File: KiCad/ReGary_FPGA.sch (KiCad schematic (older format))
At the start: 28 parts, among them U1 GW1N-UV1P5LQ100, U2 LM1117-3.3, U3 TPS73643DBV

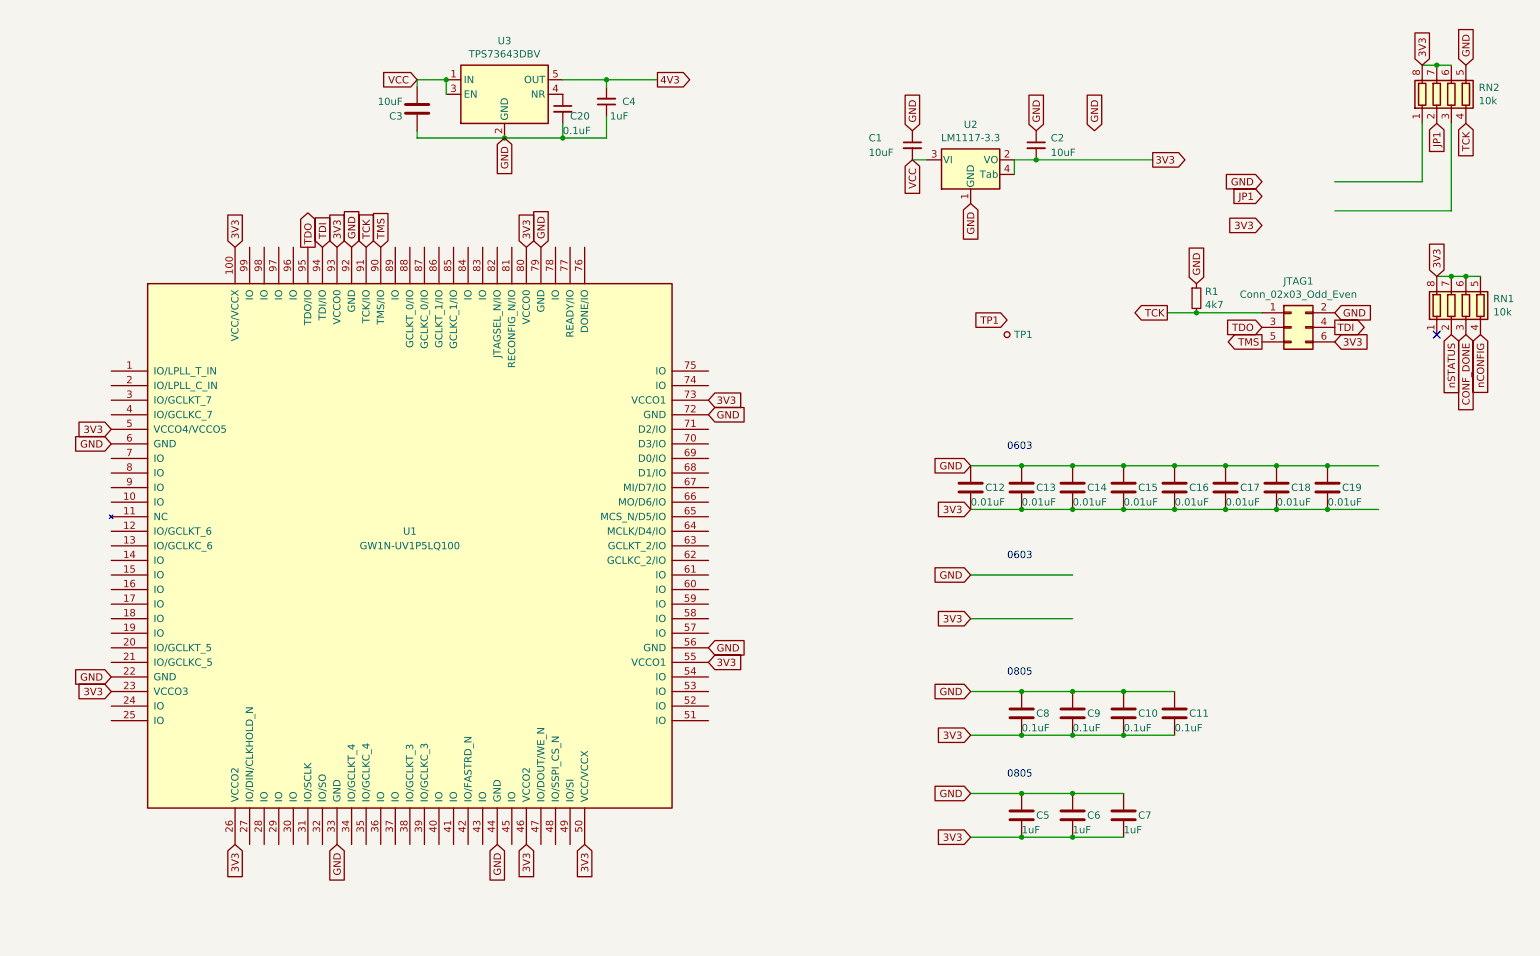
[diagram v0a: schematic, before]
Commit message: Add JP header for JTAGSEL_N, fixed JTAG as dual-purpose pins
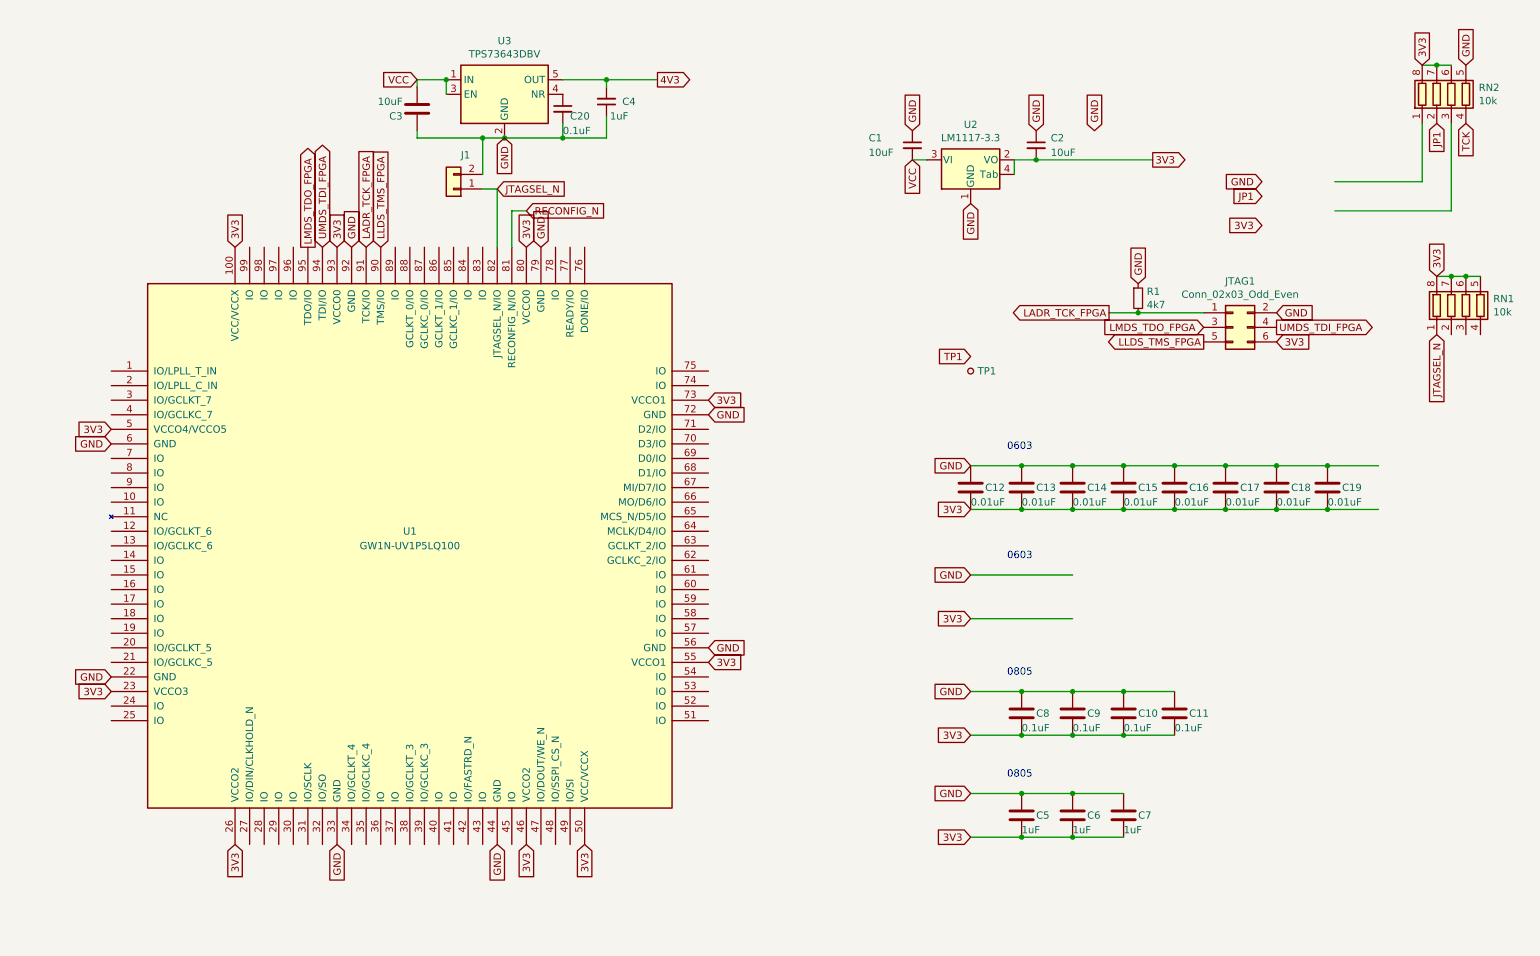
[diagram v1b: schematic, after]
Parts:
- added J1: Conn_01x02, Connector_PinHeader_2.00mm:PinHeader_1x02_P2.00mm_Vertical, symbol Connector_Generic:Conn_01x02
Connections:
- net labels added: JTAGSEL_N, LADR_TCK_FPGA, LLDS_TMS_FPGA, LMDS_TDO_FPGA, RECONFIG_N, UMDS_TDI_FPGA
- net labels removed: CONF_DONE, TDI, TDO, TMS, nCONFIG, nSTATUS
- wire segments 59 -> 65
- no-connect marks 1 -> 0
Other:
- moved on the sheet: JTAG1, R1, TP1
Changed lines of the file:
@@
 Text GLabel 9250 1950 0    50   Input ~ 0
 3V3
-Text GLabel 8800 2350 1    50   Input ~ 0
-GND
-Text GLabel 2800 2100 1    50   Input ~ 0
-TDI
-Text GLabel 3200 2100 1    50   Input ~ 0
-TMS
-Text GLabel 2700 2100 1    50   Output ~ 0
-TDO
+Text GLabel 8400 2350 1    50   Input ~ 0
+GND
 Text GLabel 10350 850  1    50   Input ~ 0
 3V3
@@
 	1    0    0    -1
 $EndComp
-Text GLabel 10650 2700 3    50   Input ~ 0
-CONF_DONE
-Text GLabel 10550 2700 3    50   Input ~ 0
-nSTATUS
-Text GLabel 10750 2700 3    50   Input ~ 0
-nCONFIG
 Text GLabel 10450 2300 1    50   Input ~ 0
 3V3
@@
 GND
 Text GLabel 10650 1250 3    50   Input ~ 0
-TCK
-Text GLabel 3100 2100 1    50   Input ~ 0
 TCK
 $Comp
@@
 	-1   0    0    1
 $EndComp
-Text GLabel 7500 2600 0    50   Input ~ 0
+Text GLabel 7250 2850 0    50   Input ~ 0
 TP1
 Wire Wire Line
@@
 L Connector:TestPoint_Small TP1
 U 1 1 655D4DC6
-P 7500 2700
-F 0 "TP1" H 7548 2700 50  0000 L CNN
-F 1 "TestPoint_Small" H 7548 2655 50  0001 L CNN
-F 2 "TestPoint:TestPoint_Pad_1.5x1.5mm" H 7700 2700 50  0001 C CNN
-F 3 "~" H 7700 2700 50  0001 C CNN
-	1    7500 2700
+P 7250 2950
+F 0 "TP1" H 7298 2950 50  0000 L CNN
+F 1 "TestPoint_Small" H 7298 2905 50  0001 L CNN
+F 2 "TestPoint:TestPoint_Pad_1.5x1.5mm" H 7450 2950 50  0001 C CNN
+F 3 "~" H 7450 2950 50  0001 C CNN
+	1    7250 2950
 	1    0    0    -1
 $EndComp
@@
 Wire Wire Line
 	10550 1250 10550 1850
-NoConn ~ 10450 2700
 $Comp
 L Device:C_Small C?
@@
 L Connector_Generic:Conn_02x03_Odd_Even JTAG1
 U 1 1 67CA7A4E
-P 9450 2650
-F 0 "JTAG1" H 9500 2967 50  0000 C CNN
-F 1 "Conn_02x03_Odd_Even" H 9500 2876 50  0000 C CNN
-F 2 "Connector_PinHeader_2.00mm:PinHeader_2x03_P2.00mm_Vertical_SMD" H 9450 2650 50  0001 C CNN
-F 3 "~" H 9450 2650 50  0001 C CNN
-	1    9450 2650
-	1    0    0    -1
-$EndComp
-Text GLabel 8600 2550 0    50   Output ~ 0
-TCK
-Text GLabel 9250 2650 0    50   Input ~ 0
-TDO
-Text GLabel 9250 2750 0    50   Output ~ 0
-TMS
-Text GLabel 9750 2550 2    50   Input ~ 0
-GND
-Text GLabel 9750 2650 2    50   Output ~ 0
-TDI
-Text GLabel 9750 2750 2    50   Input ~ 0
+P 9050 2650
+F 0 "JTAG1" H 9100 2967 50  0000 C CNN
+F 1 "Conn_02x03_Odd_Even" H 9100 2876 50  0000 C CNN
+F 2 "Connector_PinHeader_2.00mm:PinHeader_2x03_P2.00mm_Vertical_SMD" H 9050 2650 50  0001 C CNN
+F 3 "~" H 9050 2650 50  0001 C CNN
+	1    9050 2650
+	1    0    0    -1
+$EndComp
+Text GLabel 9350 2550 2    50   Input ~ 0
+GND
+Text GLabel 9350 2750 2    50   Input ~ 0
 3V3
 $Comp
@@
 	7700 1500 8500 1500
 Wire Wire Line
-	3450 1350 4050 1350
+	3450 1350 3900 1350
 Text GLabel 4050 1350 3    50   Input ~ 0
 GND
@@
 L Device:R_Small R1
 U 1 1 67F65041
-P 8800 2450
-F 0 "R1" H 8859 2496 50  0000 L CNN
-F 1 "4k7" H 8859 2405 50  0000 L CNN
-F 2 "Resistor_SMD:R_0603_1608Metric_Pad0.98x0.95mm_HandSolder" H 8800 2450 50  0001 C CNN
-F 3 "~" H 8800 2450 50  0001 C CNN
-	1    8800 2450
-	1    0    0    -1
-$EndComp
-Wire Wire Line
-	9250 2550 8800 2550
-Connection ~ 8800 2550
-Wire Wire Line
-	8800 2550 8600 2550
+P 8400 2450
+F 0 "R1" H 8459 2496 50  0000 L CNN
+F 1 "4k7" H 8459 2405 50  0000 L CNN
+F 2 "Resistor_SMD:R_0603_1608Metric_Pad0.98x0.95mm_HandSolder" H 8400 2450 50  0001 C CNN
+F 3 "~" H 8400 2450 50  0001 C CNN
+	1    8400 2450
+	1    0    0    -1
+$EndComp
+Wire Wire Line
+	8850 2550 8400 2550
+Connection ~ 8400 2550
+Wire Wire Line
+	8400 2550 8200 2550
 Wire Wire Line
 	8300 5150 8650 5150
@@
 	8300 5450 8650 5450
 Connection ~ 8300 5450
+Text GLabel 4000 1700 2    50   Input ~ 0
+JTAGSEL_N
+Text GLabel 10450 2700 3    50   Input ~ 0
+JTAGSEL_N
+$Comp
+L Connector_Generic:Conn_01x02 J1
+U 1 1 67FA6DF8
+P 3700 1700
+F 0 "J1" H 3618 1467 50  0000 C CNN
+F 1 "Conn_01x02" H 3618 1466 50  0001 C CNN
+F 2 "Connector_PinHeader_2.00mm:PinHeader_1x02_P2.00mm_Vertical" H 3700 1700 50  0001 C CNN
+F 3 "~" H 3700 1700 50  0001 C CNN
+	1    3700 1700
+	-1   0    0    1
+$EndComp
+Wire Wire Line
+	4100 2100 4100 1850
+Wire Wire Line
+	4100 1850 4200 1850
+Text GLabel 4200 1850 2    50   Input ~ 0
+RECONFIG_N
+Wire Wire Line
+	4000 2100 4000 1700
+Wire Wire Line
+	3900 1700 4000 1700
+Wire Wire Line
+	3900 1600 3900 1350
+Connection ~ 3900 1350
+Wire Wire Line
+	3900 1350 4050 1350
+Text GLabel 2800 2100 1    50   BiDi ~ 0
+UMDS_TDI_FPGA
+Text GLabel 9350 2650 2    50   Output ~ 0
+UMDS_TDI_FPGA
+Text GLabel 8850 2650 0    50   Input ~ 0
+LMDS_TDO_FPGA
+Text GLabel 2700 2100 1    50   Output ~ 0
+LMDS_TDO_FPGA
+Text GLabel 8200 2550 0    50   Output ~ 0
+LADR_TCK_FPGA
+Text GLabel 3100 2100 1    50   Input ~ 0
+LADR_TCK_FPGA
+Text GLabel 8850 2750 0    50   Output ~ 0
+LLDS_TMS_FPGA
+Text GLabel 3200 2100 1    50   Input ~ 0
+LLDS_TMS_FPGA
 $EndSCHEMATC

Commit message: More signal to pin assignments and routing
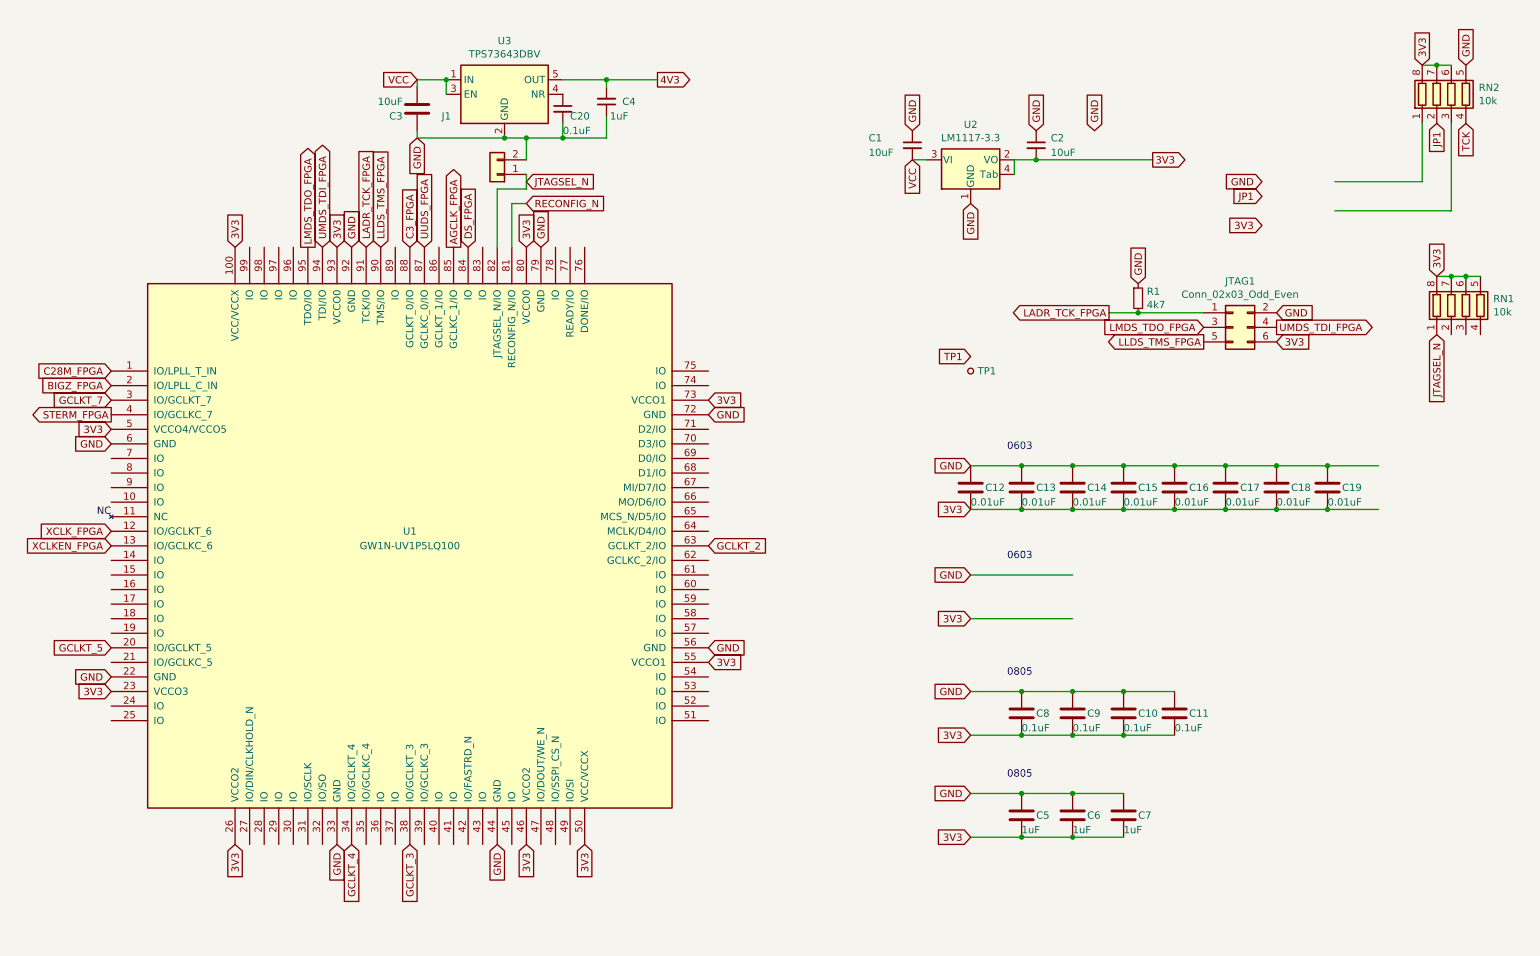
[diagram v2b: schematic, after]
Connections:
- net labels added: AGCLK_FPGA, BIGZ_FPGA, C28M_FPGA, C3_FPGA, DS_FPGA, GCLKT_2, GCLKT_3, GCLKT_4, GCLKT_5, GCLKT_7, NC, STERM_FPGA, UUDS_FPGA, XCLKEN_FPGA, XCLK_FPGA
- wire segments 65 -> 66
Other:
- moved on the sheet: J1
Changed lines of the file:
@@
 Wire Wire Line
 	7700 1500 8500 1500
-Wire Wire Line
-	3450 1350 3900 1350
-Text GLabel 4050 1350 3    50   Input ~ 0
+Text GLabel 3450 1350 3    50   Input ~ 0
 GND
 Text GLabel 5100 950  2    50   Output ~ 0
@@
 Wire Wire Line
 	3450 950  3450 1000
-Wire Wire Line
-	4050 1350 4450 1350
 Wire Wire Line
 	4750 1350 4750 1200
@@
 	8300 5450 8650 5450
 Connection ~ 8300 5450
-Text GLabel 4000 1700 2    50   Input ~ 0
+Text GLabel 4200 1650 2    50   Input ~ 0
 JTAGSEL_N
 Text GLabel 10450 2700 3    50   Input ~ 0
@@
 L Connector_Generic:Conn_01x02 J1
 U 1 1 67FA6DF8
-P 3700 1700
-F 0 "J1" H 3618 1467 50  0000 C CNN
-F 1 "Conn_01x02" H 3618 1466 50  0001 C CNN
-F 2 "Connector_PinHeader_2.00mm:PinHeader_1x02_P2.00mm_Vertical" H 3700 1700 50  0001 C CNN
-F 3 "~" H 3700 1700 50  0001 C CNN
-	1    3700 1700
+P 4000 1600
+F 0 "J1" H 4350 1200 50  0000 C CNN
+F 1 "Conn_01x02" H 3918 1366 50  0001 C CNN
+F 2 "Connector_PinHeader_2.00mm:PinHeader_1x02_P2.00mm_Vertical" H 4000 1600 50  0001 C CNN
+F 3 "~" H 4000 1600 50  0001 C CNN
+	1    4000 1600
 	-1   0    0    1
 $EndComp
-Wire Wire Line
-	4100 2100 4100 1850
-Wire Wire Line
-	4100 1850 4200 1850
-Text GLabel 4200 1850 2    50   Input ~ 0
+Text GLabel 4200 1800 2    50   Input ~ 0
 RECONFIG_N
-Wire Wire Line
-	4000 2100 4000 1700
-Wire Wire Line
-	3900 1700 4000 1700
-Wire Wire Line
-	3900 1600 3900 1350
-Connection ~ 3900 1350
-Wire Wire Line
-	3900 1350 4050 1350
 Text GLabel 2800 2100 1    50   BiDi ~ 0
 UMDS_TDI_FPGA
@@
 Text GLabel 3200 2100 1    50   Input ~ 0
 LLDS_TMS_FPGA
+Text GLabel 1350 4050 0    50   Input ~ 0
+XCLK_FPGA
+Text GLabel 3400 2100 1    50   Input ~ 0
+C3_FPGA
+Wire Wire Line
+	4200 1800 4100 1800
+Wire Wire Line
+	4100 1800 4100 2100
+Text GLabel 3500 2100 1    50   Input ~ 0
+UUDS_FPGA
+Text GLabel 3700 2100 1    50   Output ~ 0
+AGCLK_FPGA
+Wire Wire Line
+	3450 1350 4050 1350
+Wire Wire Line
+	4050 1350 4200 1350
+Wire Wire Line
+	4000 2100 4000 1700
+Wire Wire Line
+	4000 1700 4200 1700
+Wire Wire Line
+	4200 1600 4200 1700
+Wire Wire Line
+	4200 1500 4200 1350
+Connection ~ 4200 1350
+Wire Wire Line
+	4200 1350 4450 1350
+Text GLabel 3800 2100 1    50   Input ~ 0
+DS_FPGA
+Text GLabel 5450 4150 2    50   Input ~ 0
+GCLKT_2
+Text GLabel 3400 6200 3    50   Input ~ 0
+GCLKT_3
+Text GLabel 3000 6200 3    50   Input ~ 0
+GCLKT_4
+Text GLabel 1350 4850 0    50   Input ~ 0
+GCLKT_5
+Text GLabel 1350 3150 0    50   Input ~ 0
+GCLKT_7
+Text GLabel 1350 4150 0    50   Input ~ 0
+XCLKEN_FPGA
+Text Label 1350 3950 2    50   ~ 0
+NC
+Text GLabel 1350 2950 0    50   Input ~ 0
+C28M_FPGA
+Text GLabel 1350 3250 0    50   Output ~ 0
+STERM_FPGA
+Text GLabel 1350 3050 0    50   Input ~ 0
+BIGZ_FPGA
 $EndSCHEMATC
